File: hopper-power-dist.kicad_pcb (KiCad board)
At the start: 2 copper layers, 109 x 79 mm, 35 parts, among them J1 XT60PW-M, J2 XT60PW-M, J3 B2B-XH-A(LF)(SN), J4 B2B-XH-A(LF)(SN), J5 XT60PW-F, J6 XT60PW-F, J7 XT60PW-F, J8 XT60PW-F, J9 XT60PW-F, SW1 FT_Power_Switch

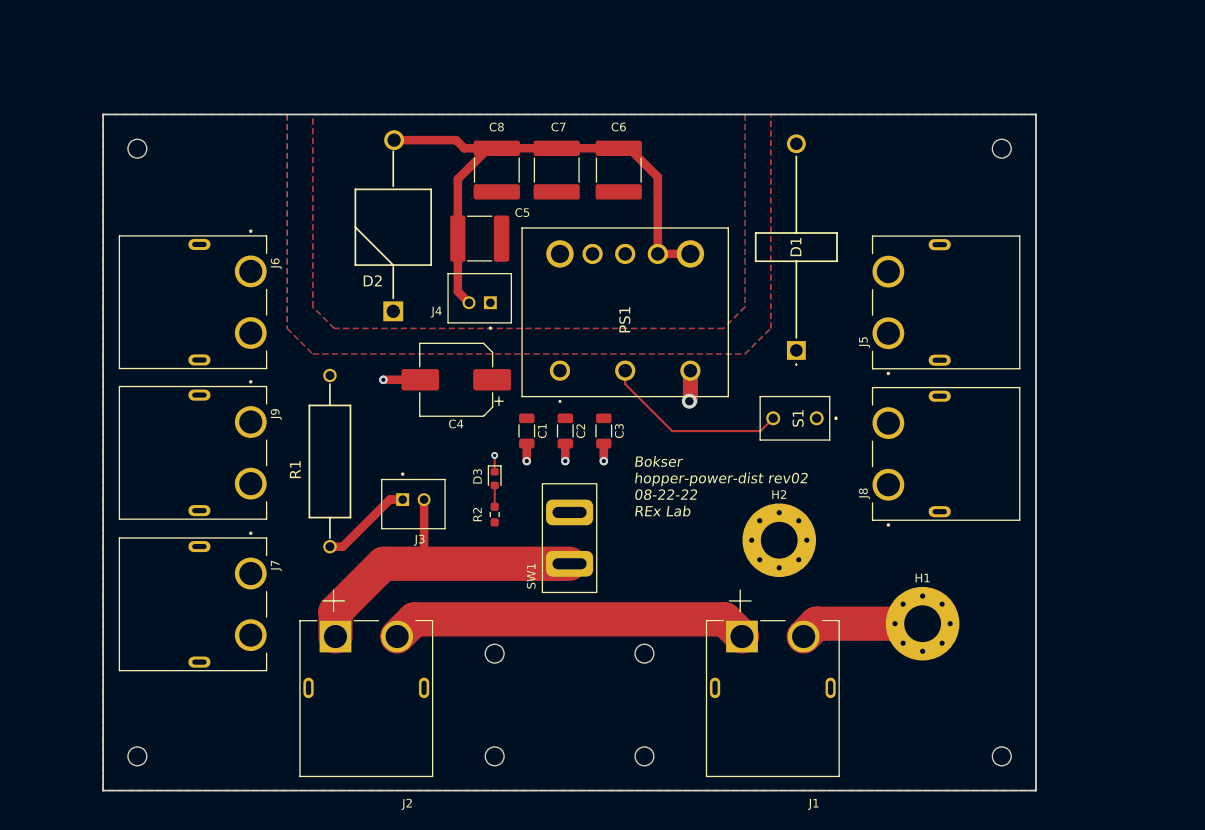
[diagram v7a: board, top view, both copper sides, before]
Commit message: Replaced DC-DC Converter and working on capacitor selection
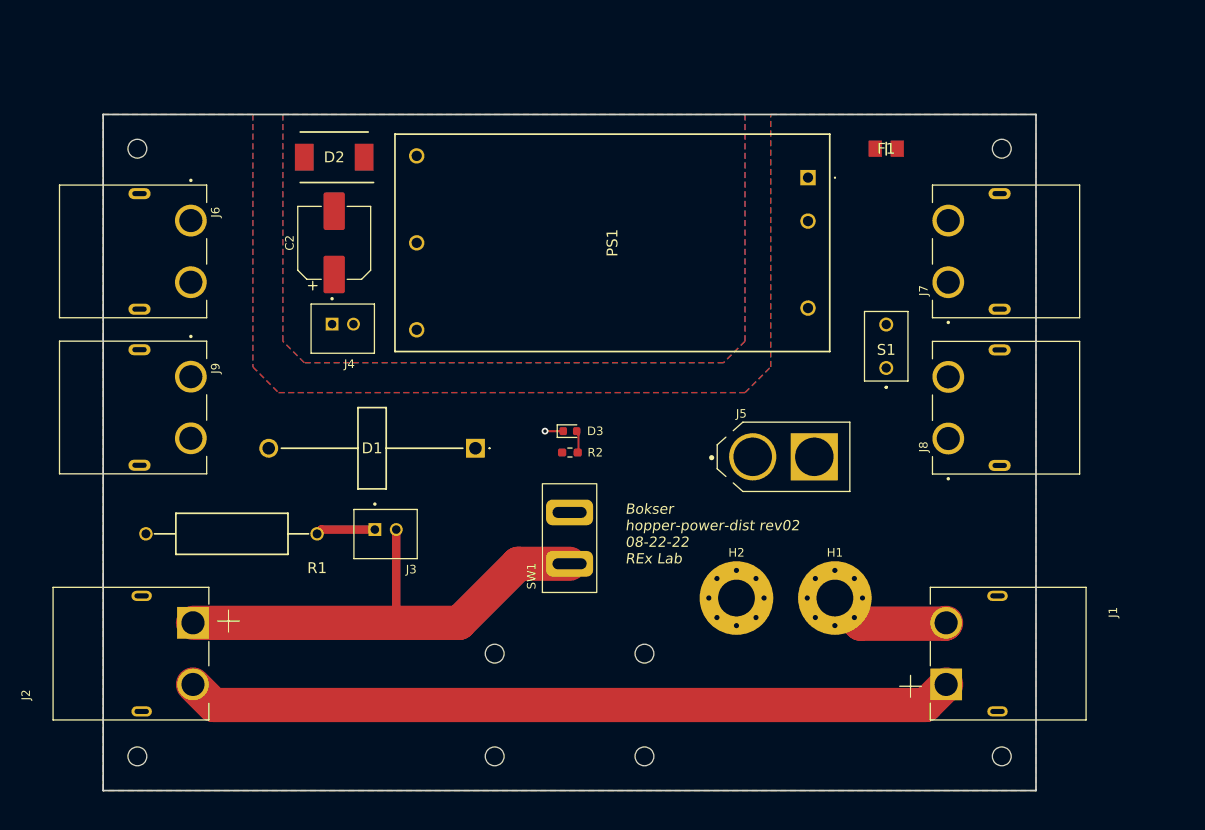
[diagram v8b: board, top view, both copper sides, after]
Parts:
- removed C1, C3: 1μF, Capacitor_SMD:C_1206_3216Metric
- removed C4: 33μF, benbokser:CP_Elec_8x10_MAL214699903E3
- removed C5, C6, C7, C8: 47μF, Capacitor_SMD:C_2220_5650Metric
- added F1: SF-1206S1000W-2, SamacSys_Parts:FUSC3216X123N, F.Cu at (146.5, 67.0)
- C2: value 1μF -> 220μF; footprint Capacitor_SMD:C_1206_3216Metric -> benbokser:CP_Elec_8x10_150CRZ
- D2: value 5KP12A -> SMDJ17A; footprint benbokser:5KP12A -> SamacSys_Parts:DIOM7959X262N
- J5: value XT60PW-F -> XT60-F; footprint XT60PW-F:AMASS_XT60PW-F -> XT60PW-F:AMASS_XT60-F
- PS1: value ULT-12_2.5-D48NM-C -> JTL6048S15; footprint SamacSys_Parts:ULT1225D48NC -> SamacSys_Parts:JTL6048S15
- moved J7 91.3 mm to (153.8, 79.0), turned to 90 degrees
- moved D1 39.2 mm to (98.5, 102.0), turned to 180 degrees
- moved PS1 36.7 mm to (137.4, 70.4), turned to -90 degrees
- moved C2 34.8 mm to (82.0, 78.0), turned to 90 degrees
- moved J1 26.6 mm to (159.5, 126.0), turned to -90 degrees
- moved J2 26.6 mm to (59.5, 126.0), turned to 90 degrees
- moved J5 21.8 mm to (134.5, 103.0), turned to 0 degrees
- moved D2 19.3 mm to (82.0, 68.0), turned to 180 degrees
- moved J4 16.2 mm to (83.0, 87.5), turned to 180 degrees
- moved R2 11.4 mm to (109.5, 102.5), turned to 180 degrees
- moved H1 10.7 mm to (140.5, 119.5)
- moved D3 10.4 mm to (109.5, 100.0), turned to 0 degrees
- moved S1 10.0 mm to (146.5, 92.6), turned to 0 degrees
- moved J6 9.18 mm to (65.2, 79.0)
- moved J8 8.84 mm to (153.8, 97.3)
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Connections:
- C2 pad 1: /HS -> Net-(C2-Pad1)
- C2 pad 2: GND -> Net-(C2-Pad2)
- D2 pad 1: Net-(PS1-Pad7) -> Net-(C2-Pad1)
- D2 pad 2: /-12V -> Net-(C2-Pad2)
- J4 pad 1: Net-(PS1-Pad7) -> Net-(C2-Pad1)
- J4 pad 2: /-12V -> Net-(C2-Pad2)
- PS1 pad 1: /HS -> Net-(C1-Pad1)
- PS1 pad 2: Net-(PS1-Pad2) -> GND
- PS1 pad 3: GND -> Net-(PS1-Pad3)
- PS1 pad 4: /-12V -> Net-(C2-Pad1)
- PS1 pad 5: /-12V -> Net-(C2-Pad2)
- S1 pad 3: Net-(PS1-Pad2) -> Net-(PS1-Pad3)
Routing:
- net /-12V: track 68.4 -> 0.00 mm
- net Net-(J1-Pad1): track 42.0 -> 90.0 mm
- net Net-(PS1-Pad2): track 21.8 -> 0.00 mm
- net Net-(J2-Pad1): track 40.1 -> 58.5 mm
- net GND: track 16.2 -> 1.93 mm, vias 6 -> 1
- net Net-(J3-Pad1): track 10.8 -> 6.96 mm
- added copper zone on F.Cu, net Net-(C2-Pad1)
- added copper zone on B.Cu, net Net-(C2-Pad2)
- removed copper zone on B.Cu, net /-12V
- removed copper zone on F.Cu, net Net-(PS1-Pad7)
